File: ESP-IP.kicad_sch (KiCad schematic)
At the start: 41 parts, among them J1 Serial and power, J2 Programming Pads, J3 Comms and power, Q1 L78M05ABDT-TR, Q2 MMBT5551L, SW1 SW_Push, SW2 SW_Push, U1 ESP32-WROOM-32U, U3 TXS0102DCU, U4 AMS1117-3.3

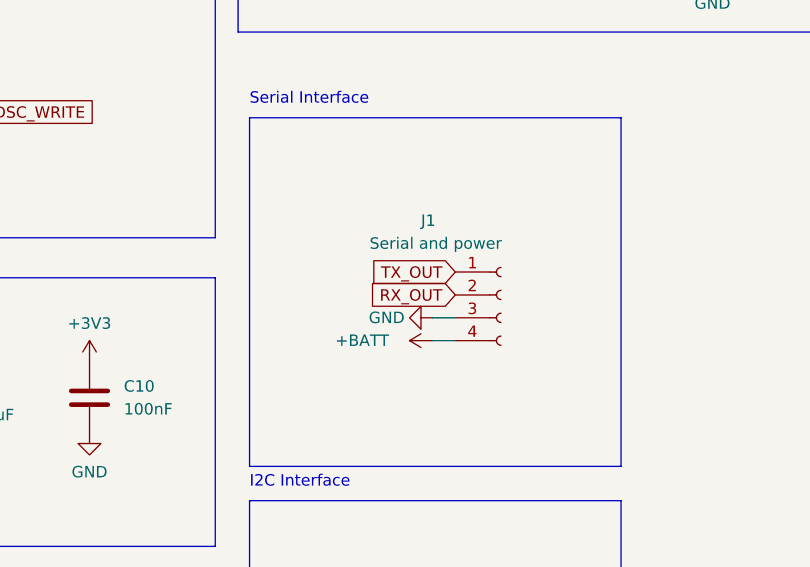
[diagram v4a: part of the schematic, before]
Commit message: chore: swap labels of rx and tx on pin socket
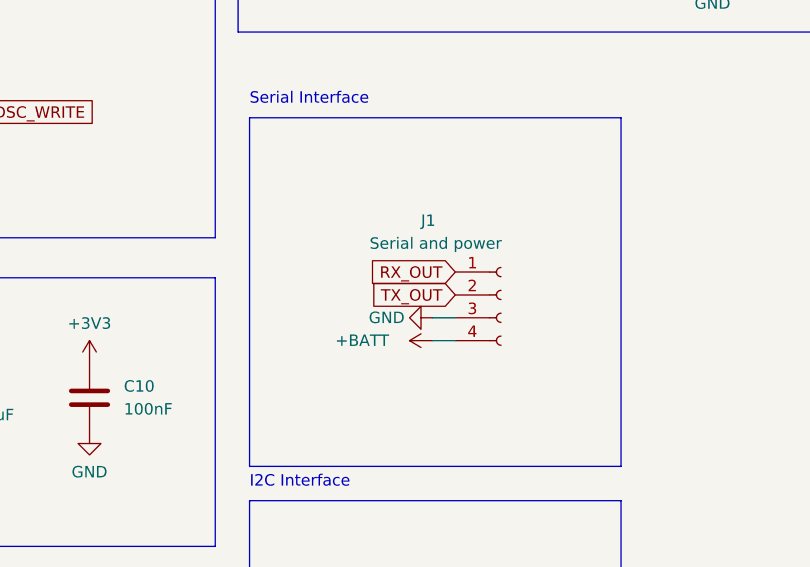
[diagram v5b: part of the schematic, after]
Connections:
- net RX_OUT: now also J1.1 (Pin_1); no longer J1.2 (Pin_2)
- net TX_OUT: now also J1.2 (Pin_2); no longer J1.1 (Pin_1)
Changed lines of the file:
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@@
-    )
-  )
-  (global_label "RX_OUT" (shape input) (at 131.445 132.715 180) (fields_autoplaced)
-    (effects (font (size 1.27 1.27)) (justify right))
-    (property "Intersheetrefs" "${INTERSHEET_REFS}" (at 121.4635 132.715 0)
-      (effects (font (size 1.27 1.27)) (justify right) hide)
     )
   )
@@
     (property "Intersheetrefs" "${INTERSHEET_REFS}" (at 188.3447 44.45 0)
       (effects (font (size 1.27 1.27)) (justify left) hide)
+    )
+  )
+  (global_label "RX_OUT" (shape input) (at 131.445 130.175 180) (fields_autoplaced)
+    (effects (font (size 1.27 1.27)) (justify right))
+    (property "Intersheetrefs" "${INTERSHEET_REFS}" (at 121.4635 130.175 0)
+      (effects (font (size 1.27 1.27)) (justify right) hide)
     )
   )
@@
     )
   )
-  (global_label "TX_OUT" (shape input) (at 131.445 130.175 180) (fields_autoplaced)
-    (effects (font (size 1.27 1.27)) (justify right))
-    (property "Intersheetrefs" "${INTERSHEET_REFS}" (at 121.7659 130.175 0)
-      (effects (font (size 1.27 1.27)) (justify right) hide)
-    )
-  )
   (global_label "WIFI_STATUS" (shape input) (at 175.26 74.93 0) (fields_autoplaced)
     (effects (font (size 1.27 1.27)) (justify left))
@@
     )
   )
+  (global_label "TX_OUT" (shape input) (at 131.445 132.715 180) (fields_autoplaced)
+    (effects (font (size 1.27 1.27)) (justify right))
+    (property "Intersheetrefs" "${INTERSHEET_REFS}" (at 121.7659 132.715 0)
+      (effects (font (size 1.27 1.27)) (justify right) hide)
+    )
+  )

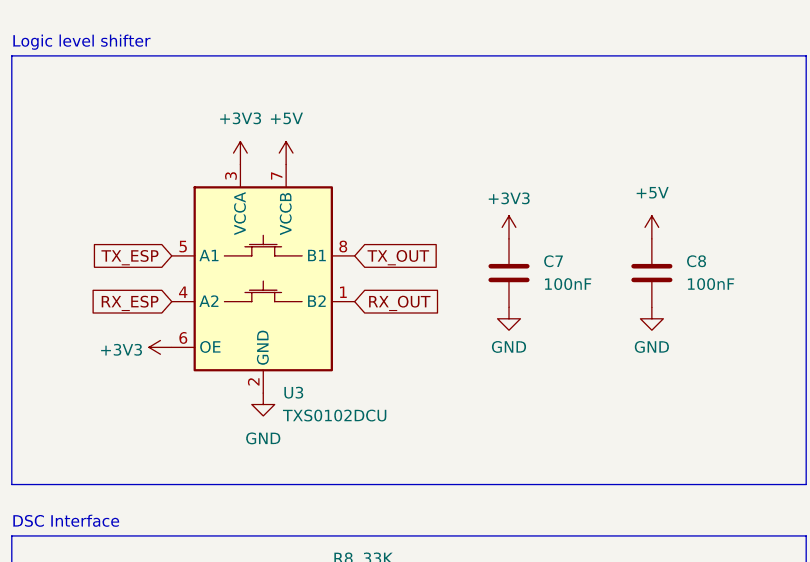
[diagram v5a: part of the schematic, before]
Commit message: chore: switch rx and tx out
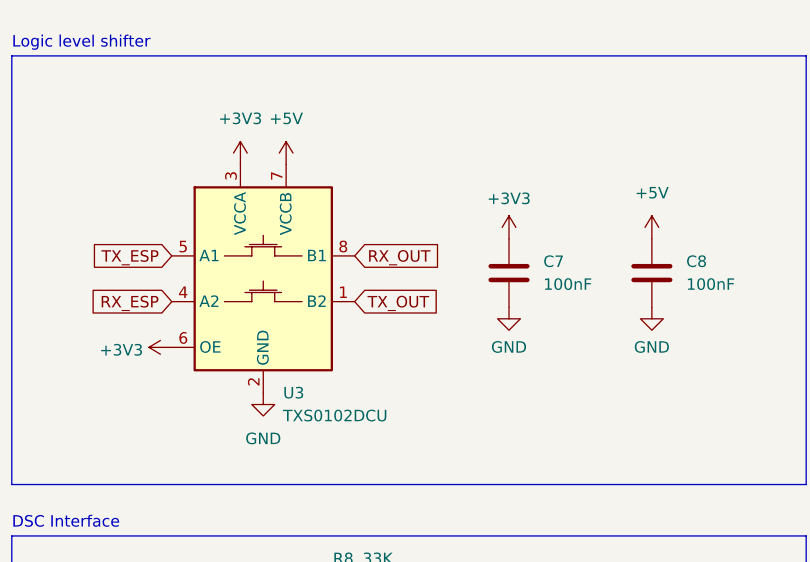
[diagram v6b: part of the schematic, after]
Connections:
- net RX_OUT: now also U3.8 (B1); no longer U3.1 (B2)
- net TX_OUT: now also U3.1 (B2); no longer U3.8 (B1)
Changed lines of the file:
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@@
     )
   )
-  (global_label "TX_OUT" (shape input) (at 54.61 38.735 0) (fields_autoplaced)
+  (global_label "RX_OUT" (shape input) (at 54.61 38.735 0) (fields_autoplaced)
     (effects (font (size 1.27 1.27)) (justify left))
-    (property "Intersheetrefs" "${INTERSHEET_REFS}" (at 64.3685 38.735 0)
+    (property "Intersheetrefs" "${INTERSHEET_REFS}" (at 64.6709 38.735 0)
       (effects (font (size 1.27 1.27)) (justify left) hide)
     )
@@
     )
   )
+  (global_label "TX_OUT" (shape input) (at 54.61 43.815 0) (fields_autoplaced)
+    (effects (font (size 1.27 1.27)) (justify left))
+    (property "Intersheetrefs" "${INTERSHEET_REFS}" (at 64.3685 43.815 0)
+      (effects (font (size 1.27 1.27)) (justify left) hide)
+    )
+  )
   (global_label "DSC_READ" (shape input) (at 71.755 90.805 0) (fields_autoplaced)
     (effects (font (size 1.27 1.27)) (justify left))
@@
       (effects (font (size 1.27 1.27)) (justify left) hide)
     )
-  )
-  (global_label "RX_OUT" (shape input) (at 54.61 43.815 0) (fields_autoplaced)
-    (effects (font (size 1.27 1.27)) (justify left))
-    (property "Intersheetrefs" "${INTERSHEET_REFS}" (at 64.6709 43.815 0)
-      (effects (font (size 1.27 1.27)) (justify left) hide)
-    )
